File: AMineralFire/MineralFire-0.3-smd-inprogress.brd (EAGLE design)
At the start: 95.9 x 68.1 mm, 86 parts, among them IC3 LM358D, Q1 20MHz, Q2 20MHz, Q3 MMBT3906LT1SMD, Q4 MMBT3906LT1SMD, Q5 MMBT3906LT1SMD, Q6 MMBT3906LT1SMD, Q7 MMBT3906LT1SMD, Q8 MMBT3906LT1SMD, Q9 MMBT3906LT1SMD, T1 200mA/40V, T2 200mA/40V, T3 200mA/40V, T4 200mA/40V, T5 200mA/40V, U1 ATMEGA328P_TQFP, U3 +12v, U4 ATMEGA328P_TQFP

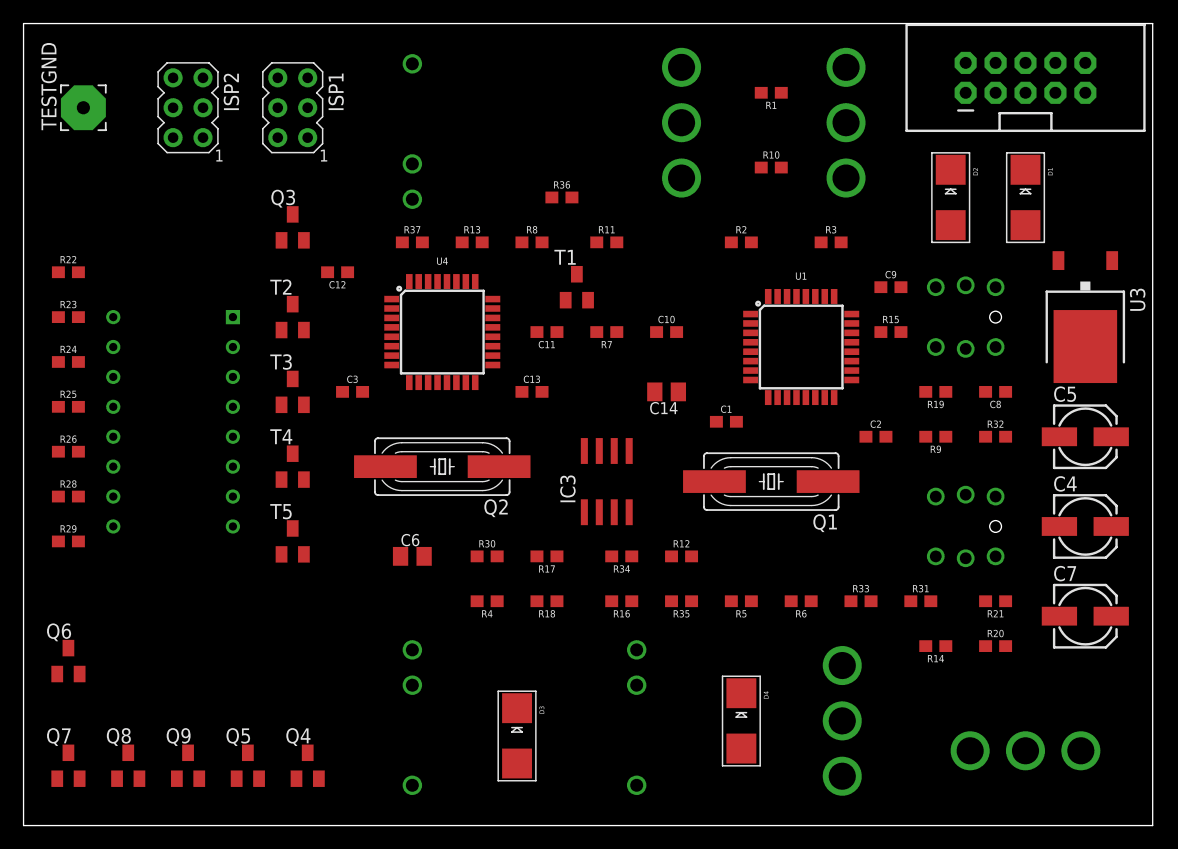
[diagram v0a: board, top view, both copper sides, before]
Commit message: Updated design to use rotary encoder
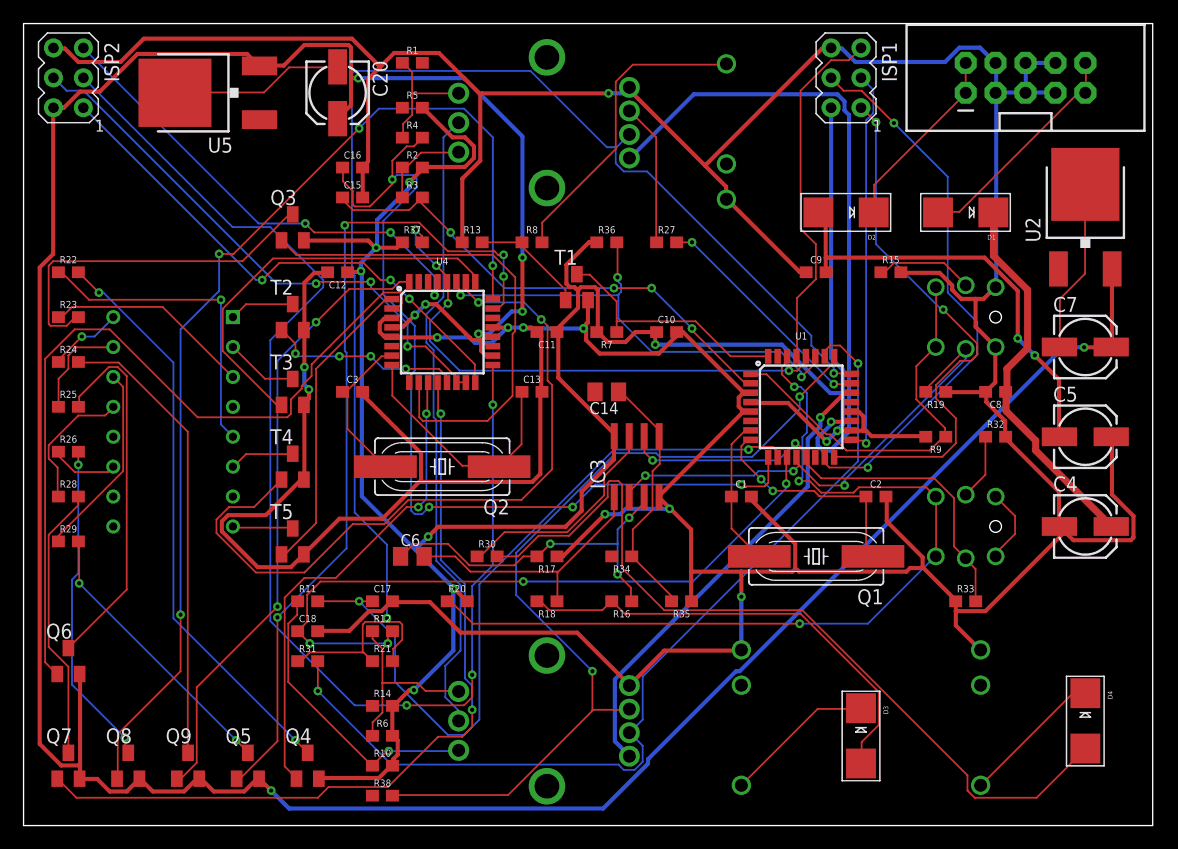
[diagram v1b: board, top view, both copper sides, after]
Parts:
- removed MODESW1, MODESW2, MODESW3, PROGSW: (no value), INSTRUO:TOGGLE_ON_OFF_ON
- removed TESTGND: WIREPAD3,81/1,1, wirepad:3,81/1,1
- removed U3: +12v, SparkFun-IC-Power:TO-252
- added C15, C16, C17, C18: 10nF, SparkFun-Capacitors:0603
- added C20: 10u, rcl:153CLV-0505
- added ENC1, ENC2: ENCODER-2LED, SparkFun-Switches:ENCODER_LED_2
- added R27, R38: 330, SparkFun-Resistors:0603
- added U2, U5: 7805, INSTRUO:V-REG
- C7: value 10uF -> 10u
- R1, R10, R14, R4: value 1k -> 10k
- R11, R12, R2, R20, R3, R5, R6: value 100k -> 10k
- R21: value 100k -> 330
- R31: value 100 -> 330
- moved R10 60.6 mm to (30.5, 5.08)
- moved R31 52.3 mm to (24.1, 14.0)
- moved R21 52.3 mm to (30.5, 14.0), turned to 0 degrees
- moved R5 50.4 mm to (33.0, 61.0), turned to 0 degrees
- moved R14 47.3 mm to (30.5, 10.2), turned to 0 degrees
- moved ISP1 47.1 mm to (69.8, 63.5)
- moved R20 45.9 mm to (36.8, 19.1)
- moved R4 39.9 mm to (33.0, 58.4), turned to 0 degrees
- moved R11 39.7 mm to (24.1, 19.1)
- moved R6 37.4 mm to (30.5, 7.62), turned to 0 degrees
- moved R3 35.8 mm to (33.0, 53.3)
- moved R1 30.6 mm to (33.0, 64.8), turned to 0 degrees
- moved D3 29.2 mm to (71.1, 7.62)
- moved D4 29.2 mm to (90.2, 8.89)
- moved TRIGOUT2 29.2 mm to (81.3, 8.42)
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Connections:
- net BUTLED renamed TRIG1
- removed net LBUTTON: BUT1.1, BUT1.2, R31.1, U1.19
- removed net T1: MODESW2.3, R11.2, U1.9
- removed net T2: MODESW2.1, R12.2, U1.2
- removed net T3: MODESW1.3, R2.2, U1.25
- removed net T4: MODESW1.1, R3.2, U1.26
- removed net T5: MODESW3.3, R5.2, U1.23
- removed net T6: MODESW3.1, R6.2, U1.24
- removed net T7: PROGSW.1, R21.2, U1.10
- removed net T8: PROGSW.3, R20.2, U1.11
- new net +12V1: U2.1
- new net +12V2: U5.1
- new net 5VDISP: C20.+, C7.+, ISP2.2, Q5.E, Q6.E, Q7.E, Q8.E, Q9.E, U2.3, U4.18, U4.20, U4.4, U5.3
- new net BUT1: ENC1.SW, U1.19
- new net BUT2: ENC2.SW, U1.22
- new net BUT3: BUT1.1, BUT1.2, R20.1, U1.30
- new net B_TRIG1: R5.1
- new net B_TRIG2: R14.1
- new net ENC1-G: R27.2, U1.23
- new net ENC1-R: ENC1.+R, R21.1, R21.2, R31.1, U1.24
- new net ENC1_TERMA: C15.1, R3.2, U1.2
- new net ENC1_TERMB: C16.1, R4.2, U1.9
- new net ENC2-G: ENC2.+G, R38.2, U1.25
- new net ENC2-R: ENC2.+R, R31.2, U1.26
- new net ENC2_TERMA: C17.1, R11.2, U1.10
- new net ENC2_TERMB: C18.1, R12.2, U1.11
- new net GND1: C7.-, U2.4
- new net GND2: C20.-, U5.4
- new net N$27: ENC2.A, R10.1, R11.1
- new net N$28: ENC2.B, R12.1, R6.1
- new net N$29: BUT1.3, BUT1.4
- new net N$30: ENC1.+G, R27.1
- new net N$35: R38.1
- net +12V: no longer U3.1
- net +5V: now also R10.2, R14.2, R2.2, R20.2, R5.2, R6.2; no longer C7.+, ISP2.2, Q5.E, Q6.E, Q7.E, Q8.E, Q9.E, R11.1, R12.1, R2.1, R20.1, R21.1, R3.1, R31.2, R5.1, R6.1, U3.2, U4.18, U4.20, U4.4
- net GND: now also C15.2, C16.2, C17.2, C18.2, ENC1.GND, ENC2.GND; no longer BUT1.3, BUT1.4, C7.-, R1.2, R10.2, R14.2, R4.2, TESTGND.1, U3.3
- net N$12: now also ENC1.B, R1.1, R4.1; no longer MODESW2.2, R10.1
- net N$3: now also ENC1.C, ENC2.C; no longer MODESW1.2, R1.1
- net N$4: now also R1.2; no longer MODESW3.2, R4.1
- net N$6: now also ENC1.A, R2.1, R3.1; no longer PROGSW.2, R14.1
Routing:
- net GND: track 0.00 -> 477.5 mm, vias 0 -> 10
- net 5VDISP: track 0.00 -> 266.4 mm, vias 0 -> 8
- net +5V: track 0.00 -> 210.3 mm, vias 0 -> 9
- net ENC1-R: track 0.00 -> 120.6 mm, vias 0 -> 2
- net SCK2: track 0.00 -> 107.6 mm, vias 0 -> 3
- net C-SEGF: track 0.00 -> 91.3 mm, vias 0 -> 4
- net ENC1_TERMB: track 0.00 -> 79.8 mm, vias 0 -> 4
- net ENC2-R: track 0.00 -> 79.7 mm, vias 0 -> 2
- net BUT3: track 0.00 -> 74.6 mm, vias 0 -> 3
- net ENC2-G: track 0.00 -> 74.4 mm, vias 0 -> 2
- net N$22: track 0.00 -> 71.1 mm
- net C-SEGA: track 0.00 -> 71.1 mm, vias 0 -> 4
- net C-SEGG: track 0.00 -> 69.4 mm
- net C-SEGC: track 0.00 -> 68.9 mm, vias 0 -> 2
- net ENC2_TERMA: track 0.00 -> 64.6 mm, vias 0 -> 2
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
